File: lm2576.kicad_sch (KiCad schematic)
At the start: 8 parts

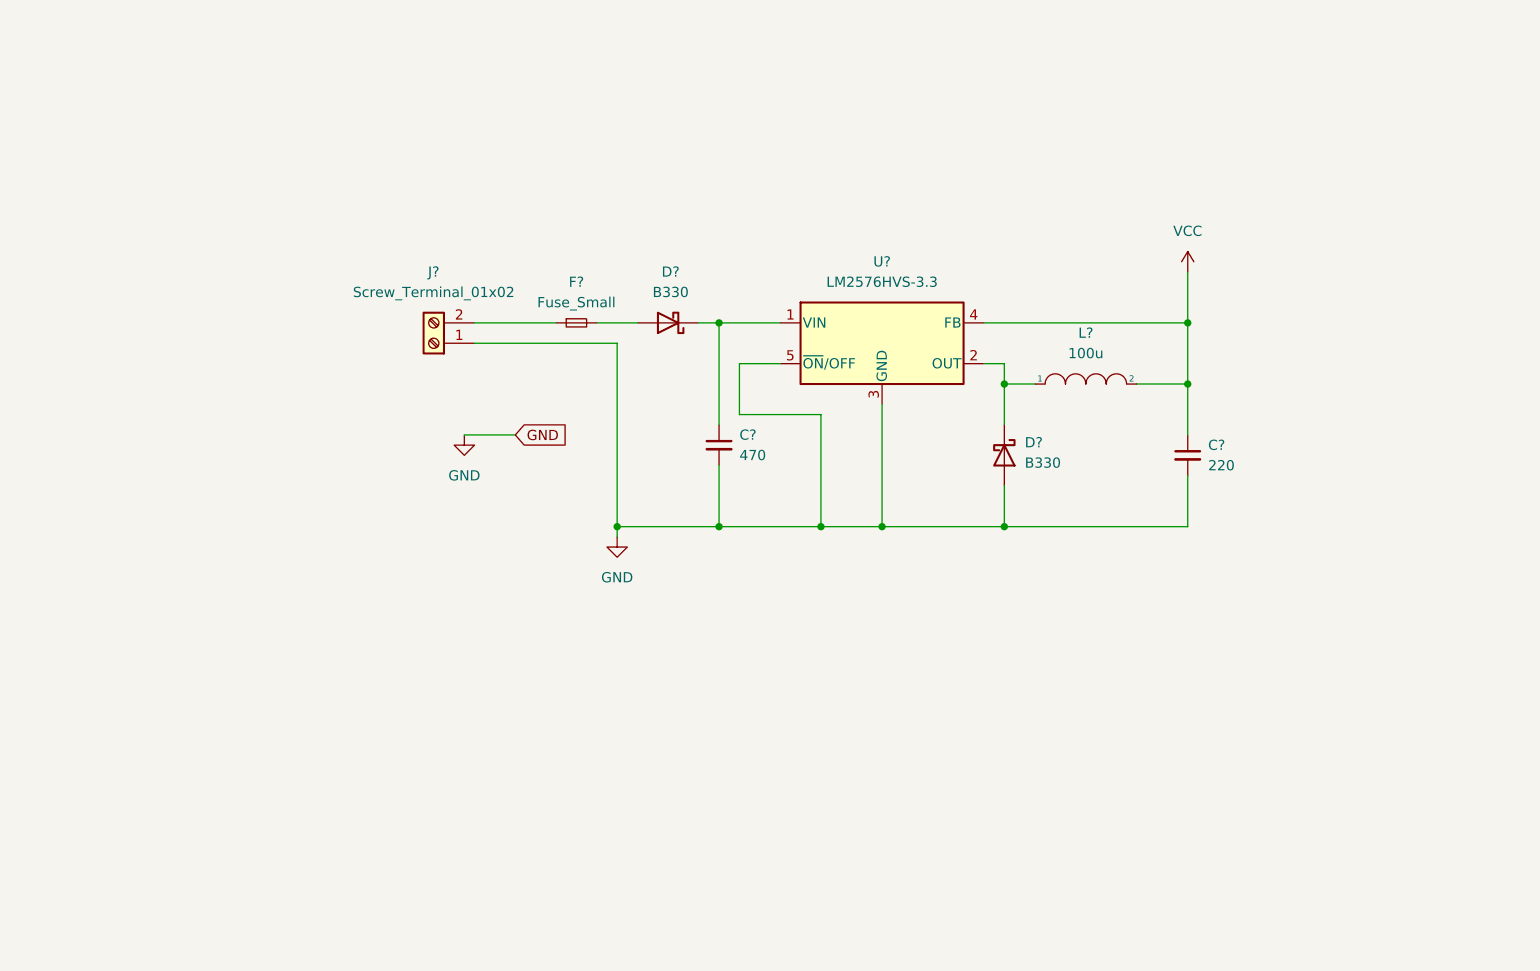
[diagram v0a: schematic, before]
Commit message: Esquema con comentarios
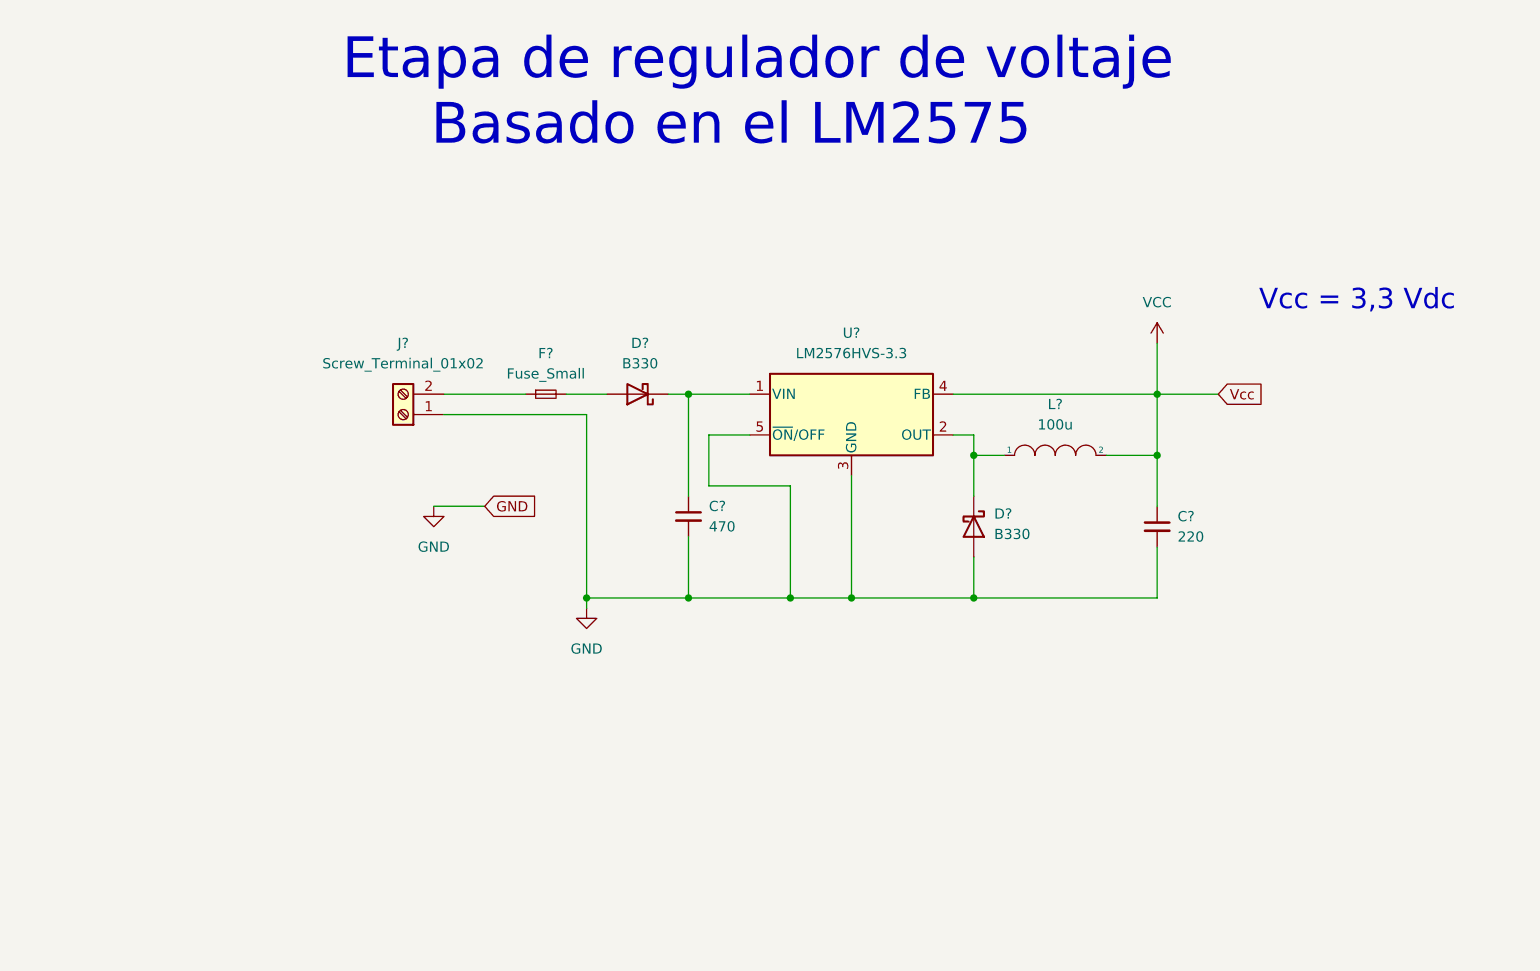
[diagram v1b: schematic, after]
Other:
- note added: "Etapa de regulador de voltaje Basado en el LM2575"
- note added: "Vcc = 3,3 Vdc"
- moved on the sheet: C?, D?, F?, J?, L?, U?

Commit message: update esq raiz
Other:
- note added: "Etapa: Regulador de voltaje Basado en el LM2575"
- note removed: "Etapa de regulador de voltaje Basado en el LM2575"
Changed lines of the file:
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@@
   (junction (at 167.64 119.38) (diameter 0) (color 0 0 0 0)
+  )
+  (junction (at 190.5 119.38) (diameter 0) (color 0 0 0 0)
   )
   (junction (at 144.78 119.38) (diameter 0) (color 0 0 0 0)
@@
     (stroke (width 0) (type default) (color 0 0 0 0))
   )
-  (wire (pts (xy 100.33 107.95) (xy 106.68 107.95))
-    (stroke (width 0) (type default) (color 0 0 0 0))
-  )
   (wire (pts (xy 190.5 93.98) (xy 190.5 101.6))
     (stroke (width 0) (type default) (color 0 0 0 0))
@@
     (stroke (width 0) (type default) (color 0 0 0 0))
   )
+  (wire (pts (xy 190.5 93.98) (xy 200.66 93.98))
+    (stroke (width 0) (type default) (color 0 0 0 0))
+  )
   (wire (pts (xy 101.6 96.52) (xy 119.38 96.52))
     (stroke (width 0) (type default) (color 0 0 0 0))
   )
   (wire (pts (xy 132.08 93.98) (xy 139.7 93.98))
-    (stroke (width 0) (type default) (color 0 0 0 0))
-  )
-  (wire (pts (xy 190.5 93.98) (xy 198.12 93.98))
     (stroke (width 0) (type default) (color 0 0 0 0))
   )
@@
   )
   (wire (pts (xy 152.4 104.14) (xy 152.4 119.38))
+    (stroke (width 0) (type default) (color 0 0 0 0))
+  )
+  (wire (pts (xy 190.5 119.38) (xy 198.12 119.38))
     (stroke (width 0) (type default) (color 0 0 0 0))
   )
@@
     (effects (font (size 2.54 2.54)) (justify left bottom))
   )
-  (text "Etapa de regulador de voltaje\n     Basado en el LM2575"
-    (at 88.9 63.5 0)
-    (effects (font (size 5.08 5.08)) (justify left bottom))
+  (text "Etapa: Regulador de voltaje\n     Basado en el LM2575"
+    (at 93.98 63.5 0)
+    (effects (font (size 5.08 5.08) (thickness 1.016) bold) (justify left bottom))
   )
-  (global_label "Vcc" (shape input) (at 198.12 93.98 0) (fields_autoplaced)
+  (hierarchical_label "gnd" (shape input) (at 198.12 119.38 0)
     (effects (font (size 1.27 1.27)) (justify left))
-    (property "Referencias entre hojas" "${INTERSHEET_REFS}" (id 0) (at 203.7988 93.9006 0)
-      (effects (font (size 1.27 1.27)) (justify left) hide)
-    )
   )
-  (global_label "GND" (shape input) (at 106.68 107.95 0) (fields_autoplaced)
+  (hierarchical_label "Vcc" (shape input) (at 200.66 93.98 0)
     (effects (font (size 1.27 1.27)) (justify left))
-    (property "Intersheet References" "${INTERSHEET_REFS}" (id 0) (at 112.9636 107.8706 0)
-      (effects (font (size 1.27 1.27)) (justify left) hide)
-    )
   )
   (symbol (lib_id "pspice:INDUCTOR") (at 177.8 101.6 0) (unit 1)
@@
     (pin "2")
   )
-  (symbol (lib_id "power:GND") (at 100.33 107.95 0) (unit 1)
-    (in_bom yes) (on_board yes) (fields_autoplaced)
-    (property "Reference" "#PWR?" (id 0) (at 100.33 114.3 0)
-      (effects (font (size 1.27 1.27)) hide)
-    )
-    (property "Value" "GND" (id 1) (at 100.33 113.03 0))
-    (property "Footprint" "" (id 2) (at 100.33 107.95 0)
-      (effects (font (size 1.27 1.27)) hide)
-    )
-    (property "Datasheet" "" (id 3) (at 100.33 107.95 0)
-      (effects (font (size 1.27 1.27)) hide)
-    )
-    (pin "1")
-  )
   (symbol (lib_id "Connector:Screw_Terminal_01x02") (at 96.52 96.52 180) (unit 1)

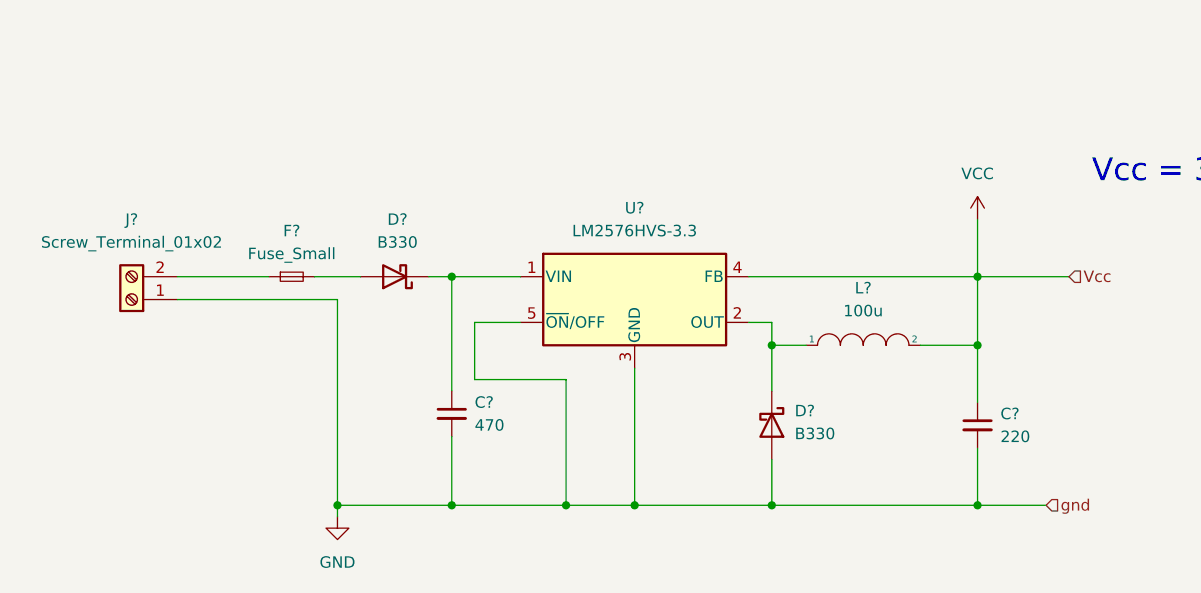
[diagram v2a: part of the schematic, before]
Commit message: add salidas separadas 1,2,3
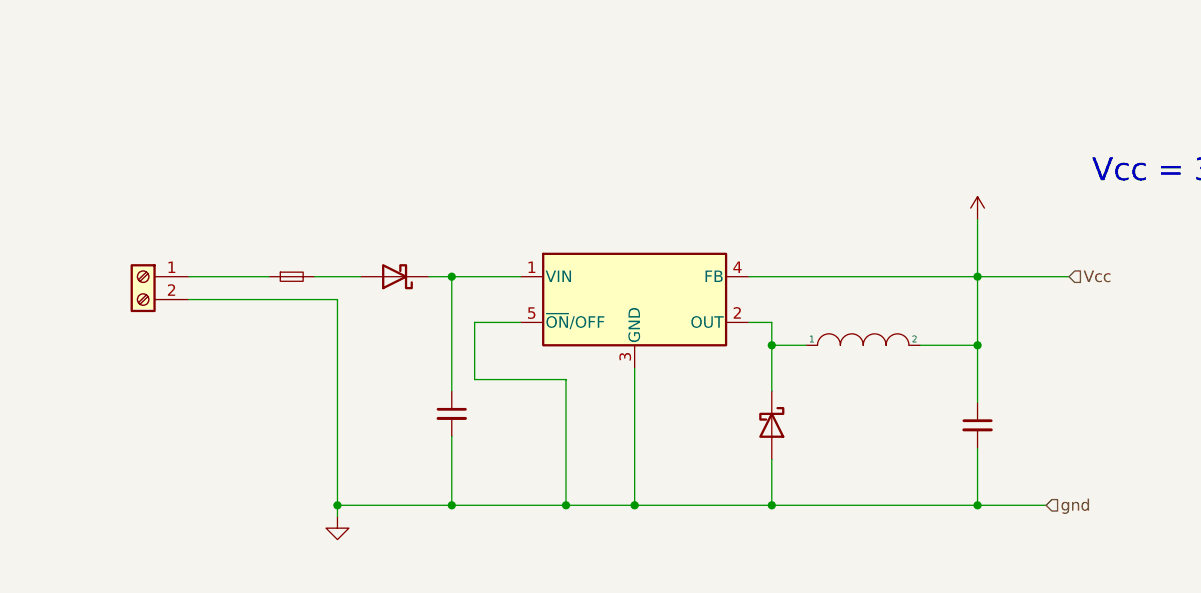
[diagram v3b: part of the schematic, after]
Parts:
- ?: renamed from L?; value 100u -> (none); footprint Inductor_SMD:L_TDK_SLF10165 -> (none)
- ?: renamed from J?; value Screw_Terminal_01x02 -> (none); footprint TerminalBlock:TerminalBlock_bornier-2_P5.08mm -> (none)
- ? (x2): renamed from D?; value B330 -> (none); footprint Diode_SMD:D_0402_1005Metric -> (none)
- ?: renamed from F?; value Fuse_Small -> (none); footprint Fuse:Fuse_0805_2012Metric -> (none)
- ?: renamed from C?; value 470 -> (none); footprint Capacitor_SMD:C_Elec_10x10.2 -> (none)
- ?: renamed from C?; value 220 -> (none); footprint Capacitor_SMD:C_Elec_6.3x7.7 -> (none)
- ?: renamed from U?; value LM2576HVS-3.3 -> (none); footprint Package_TO_SOT_SMD:TO-263-5_TabPin3 -> (none)
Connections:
- net GND: now also ?.2 (Pin_2); no longer ?.1 (Pin_1)
- net at ?.1: now also ?.1 (Pin_1); no longer ?.2 (Pin_2)
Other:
- company: (none) -> INTEAMBI

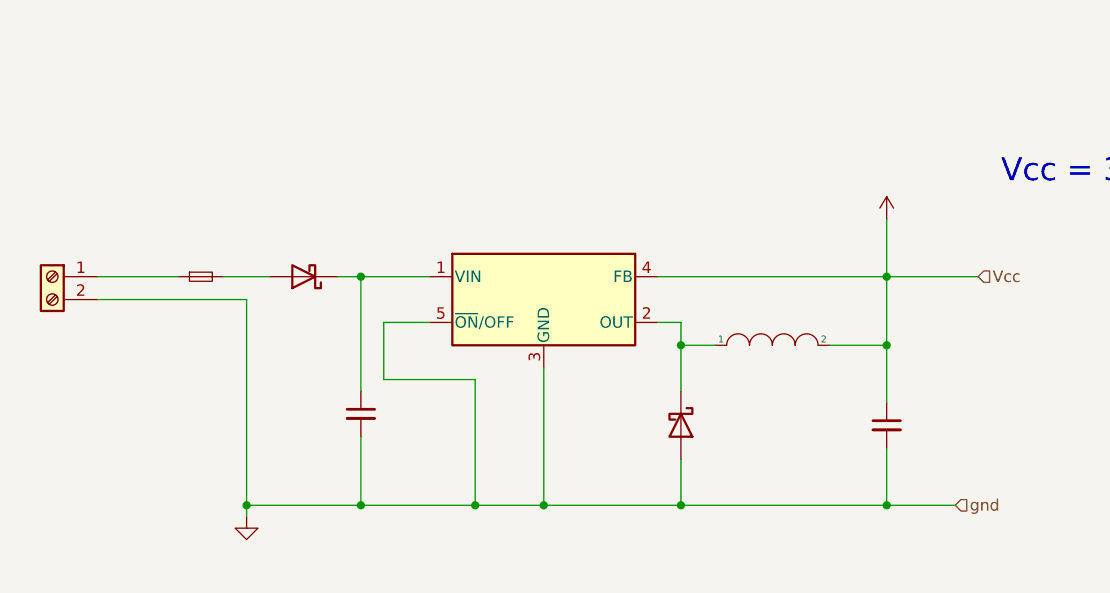
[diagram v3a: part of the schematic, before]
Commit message: add entradas separadas
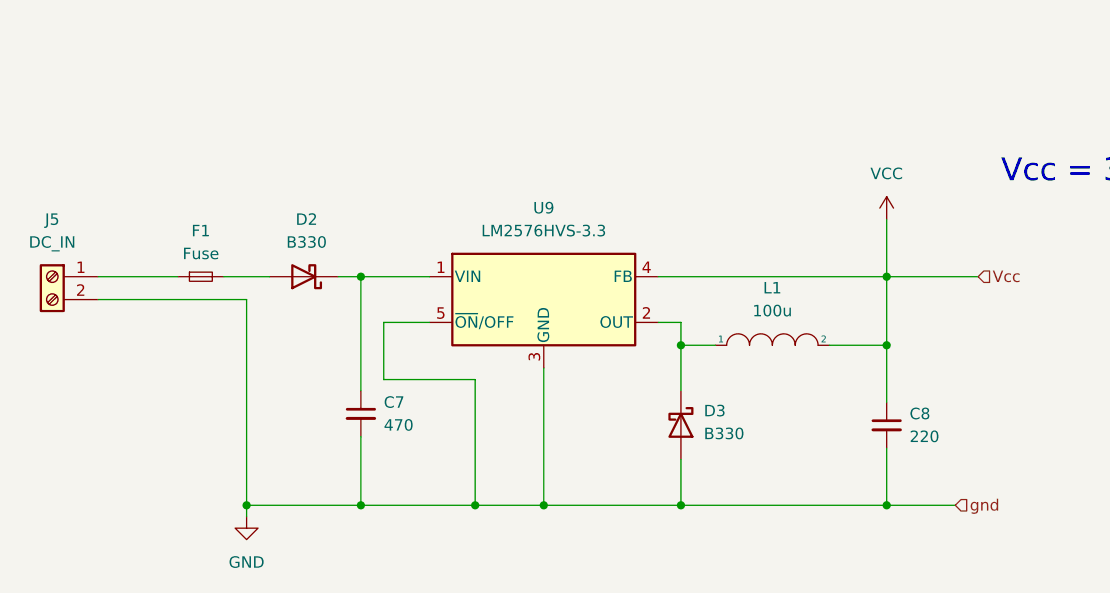
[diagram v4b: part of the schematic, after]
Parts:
- C7: renamed from ?; value (none) -> 470; footprint (none) -> Capacitor_SMD:C_Elec_10x10.2
- C8: renamed from ?; value (none) -> 220; footprint (none) -> Capacitor_SMD:C_Elec_6.3x7.7
- D2, D3: renamed from ?; value (none) -> B330; footprint (none) -> Diode_SMD:D_0402_1005Metric
- F1: renamed from ?; value (none) -> Fuse; footprint (none) -> Fuse:Fuse_0805_2012Metric
- J5: renamed from ?; value (none) -> DC_IN; footprint (none) -> TerminalBlock:TerminalBlock_bornier-2_P5.08mm
- L1: renamed from ?; value (none) -> 100u; footprint (none) -> Inductor_SMD:L_TDK_SLF10165
- U9: renamed from ?; value (none) -> LM2576HVS-3.3; footprint (none) -> Package_TO_SOT_SMD:TO-263-5_TabPin3
